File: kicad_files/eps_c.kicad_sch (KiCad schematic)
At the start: 34 parts, among them J13 5051101592, Q5 TEMT6000X01, U17 MCP3427-xUN, U18 BQ25570

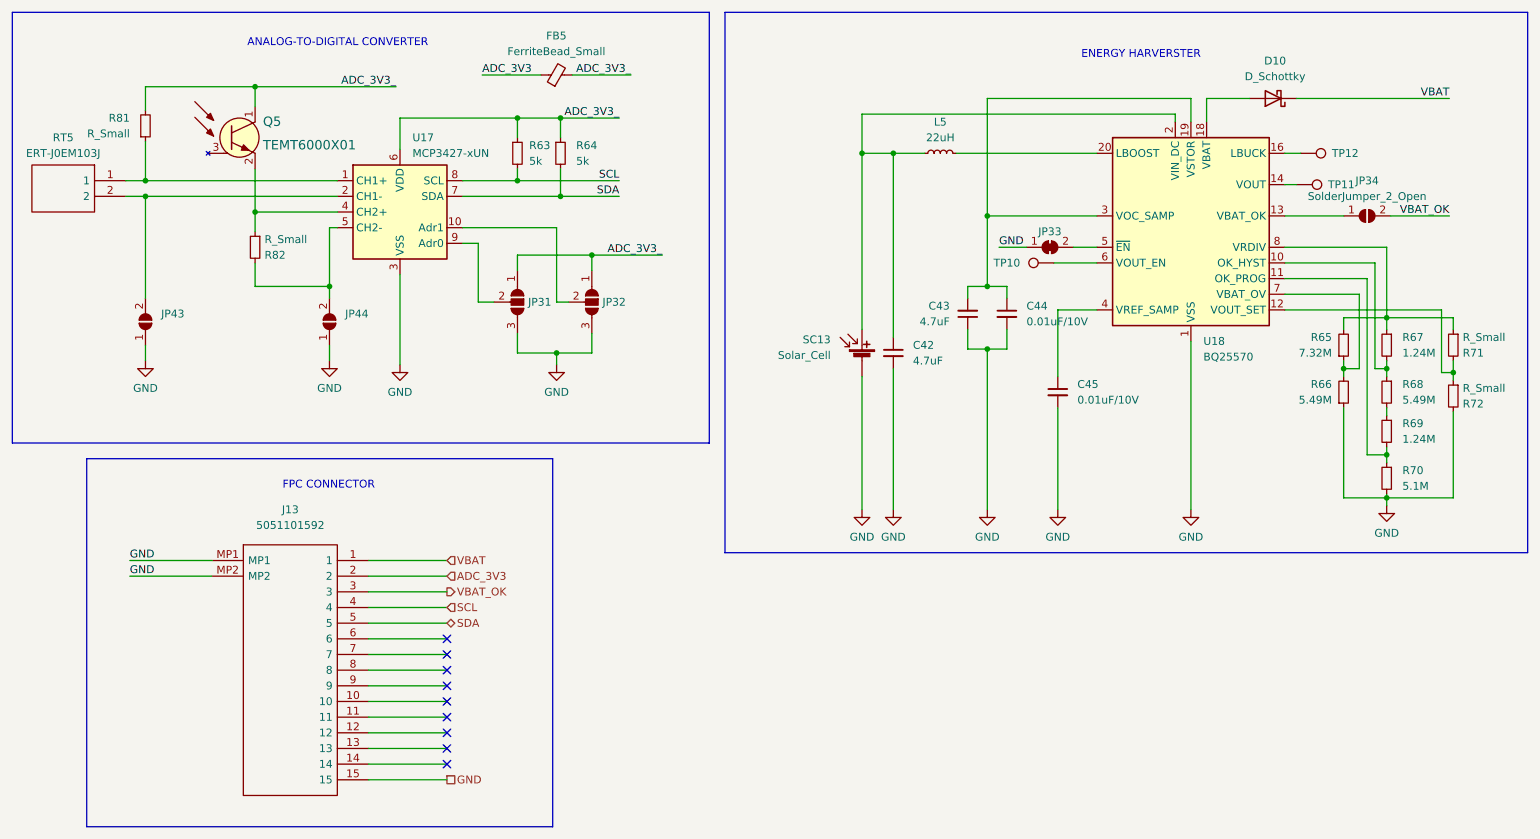
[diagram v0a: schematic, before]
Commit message: update components values
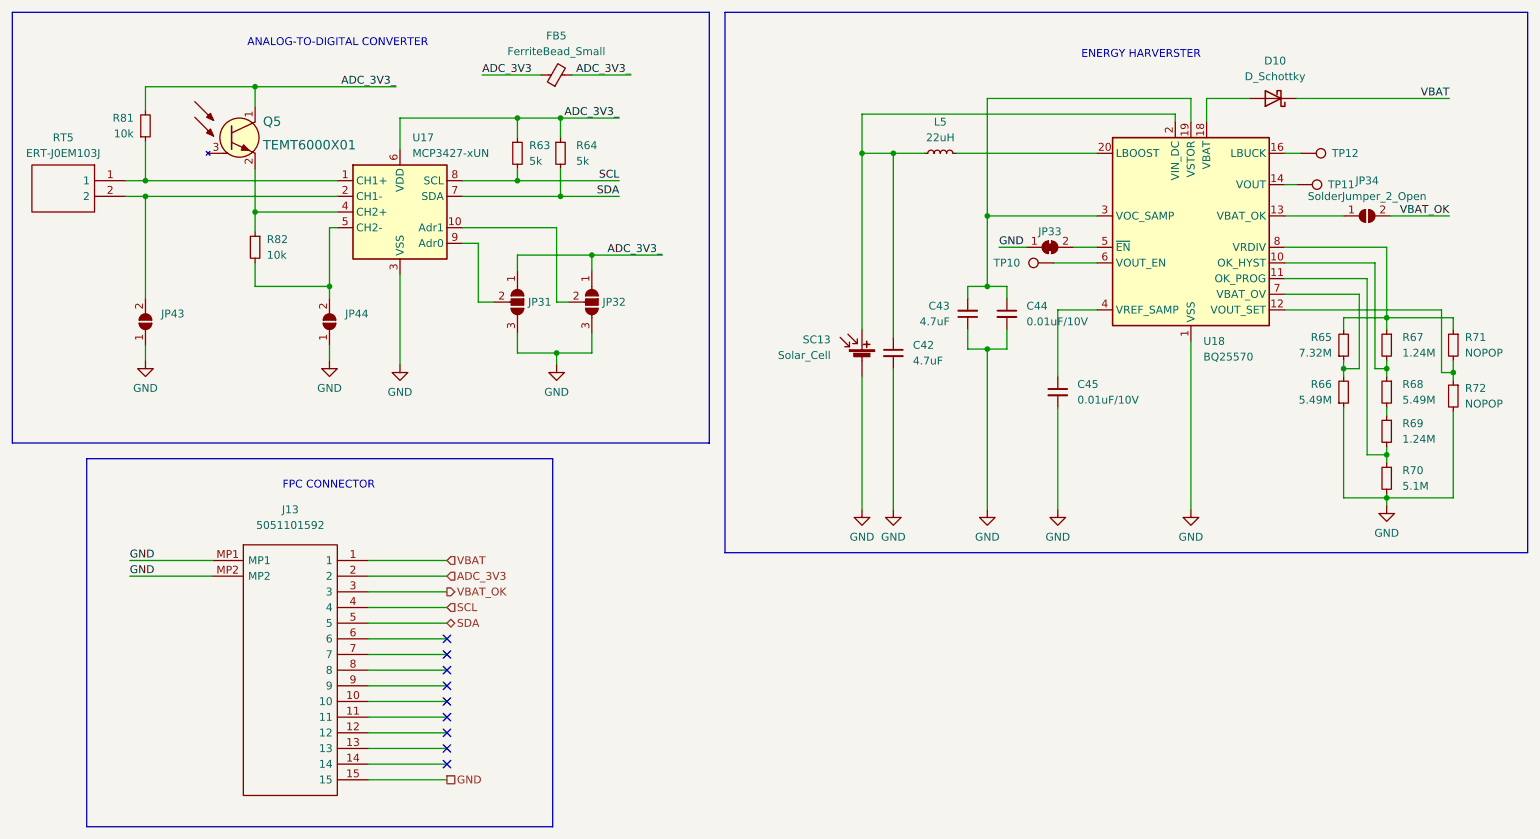
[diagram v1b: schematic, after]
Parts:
- R71, R72: value R_Small -> NOPOP
- R81, R82: value R_Small -> 10k
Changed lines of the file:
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@@
   (symbol (lib_id "Device:R_Small") (at 46.355 57.785 0) (mirror x) (unit 1)
     (in_bom yes) (on_board yes) (fields_autoplaced)
-    (property "Reference" "R81" (id 0) (at 43.815 56.5149 0)
-      (effects (font (size 1.27 1.27)) (justify right))
-    )
-    (property "Value" "R_Small" (id 1) (at 43.815 59.0549 0)
+    (property "Reference" "R81" (id 0) (at 44.45 56.5149 0)
+      (effects (font (size 1.27 1.27)) (justify right))
+    )
+    (property "Value" "10k" (id 1) (at 44.45 59.0549 0)
       (effects (font (size 1.27 1.27)) (justify right))
     )
@@
   (symbol (lib_id "Device:R_Small") (at 258.445 93.345 0) (mirror y) (unit 1)
     (in_bom yes) (on_board yes) (fields_autoplaced)
-    (property "Reference" "R71" (id 0) (at 259.969 94.6151 0)
-      (effects (font (size 1.27 1.27)) (justify right))
-    )
-    (property "Value" "R_Small" (id 1) (at 259.969 92.0751 0)
+    (property "Reference" "R71" (id 0) (at 260.35 92.0749 0)
+      (effects (font (size 1.27 1.27)) (justify right))
+    )
+    (property "Value" "NOPOP" (id 1) (at 260.35 94.6149 0)
       (effects (font (size 1.27 1.27)) (justify right))
     )
@@
   (symbol (lib_id "Device:R_Small") (at 258.445 101.6 0) (mirror y) (unit 1)
     (in_bom yes) (on_board yes) (fields_autoplaced)
-    (property "Reference" "R72" (id 0) (at 259.969 102.8701 0)
-      (effects (font (size 1.27 1.27)) (justify right))
-    )
-    (property "Value" "R_Small" (id 1) (at 259.969 100.3301 0)
+    (property "Reference" "R72" (id 0) (at 260.35 100.3299 0)
+      (effects (font (size 1.27 1.27)) (justify right))
+    )
+    (property "Value" "NOPOP" (id 1) (at 260.35 102.8699 0)
       (effects (font (size 1.27 1.27)) (justify right))
     )
@@
   (symbol (lib_id "Device:R_Small") (at 64.135 77.47 0) (mirror y) (unit 1)
     (in_bom yes) (on_board yes) (fields_autoplaced)
-    (property "Reference" "R82" (id 0) (at 65.659 78.7401 0)
-      (effects (font (size 1.27 1.27)) (justify right))
-    )
-    (property "Value" "R_Small" (id 1) (at 65.659 76.2001 0)
-      (effects (font (size 1.27 1.27)) (justify right))
-    )
+    (property "Reference" "R82" (id 0) (at 66.04 76.1999 0)
+      (effects (font (size 1.27 1.27)) (justify right))
+    )
+    (property "Value" "10k" (id 1) (at 66.04 78.7399 0)
+      (effects (font (size 1.27 1.27)) (justify right))
+    )
